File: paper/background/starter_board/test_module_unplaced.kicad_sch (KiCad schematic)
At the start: 15 parts, among them J1 Barrel_Jack_12V, M1 ERM_Motor, M2 Stepper_4wire, M3 Servo_3pin, U1 D24V22F5_Buck, U2 Pi_Pico_W, U3 DRV2605L_Breakout, U4 DRV8871_Breakout, U5 Tic_T500, U6 Waveshare_2CH_RS232

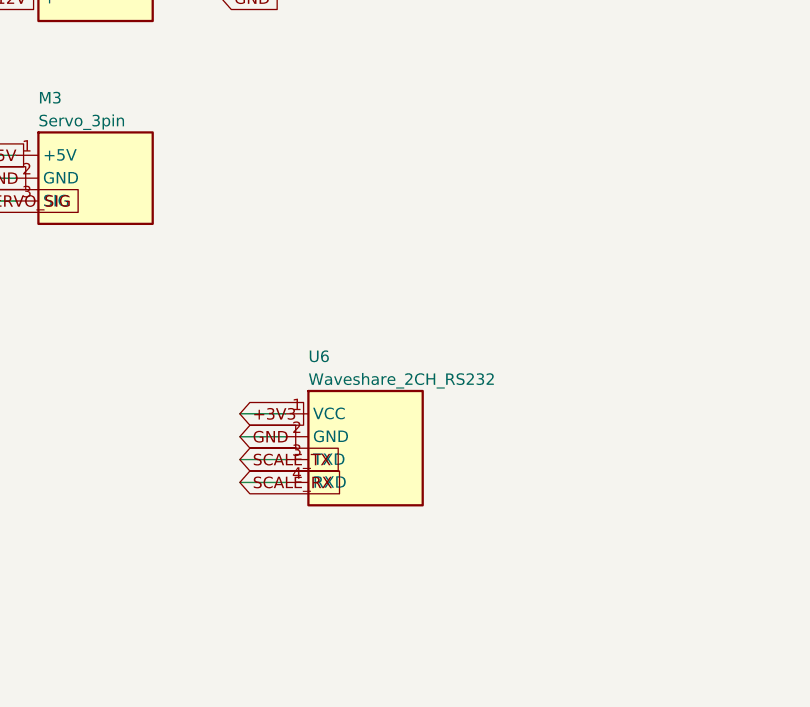
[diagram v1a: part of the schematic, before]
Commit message: Fix U6 RS-232 module footprint: restore 2x20 receptacle (mid-body 4-pin header was unpluggable)
@lbwinters caught that the generated layout placed the Waveshare
Pico-2CH-RS232 module's pin holes in the middle of its 21x52 mm body,
which would make the physical module impossible to plug in. The PR #100
alignment had adopted that PR's bench-symbol abstraction ("only its
4-pin TTL header reaches the Pico") literally, but the module's own
schematic (hardware/vendor-files/waveshare-pico-2ch-rs232) shows no
such header exists: its TTL signals live only on its 2x20
Pico-form-factor header.

U6 is again the 2x20 side receptacle the module actually plugs onto
(two real PinHeader_1x20 columns at the Pico's 17.78 mm row spacing,
as the pre-PR#100 J2 was), keeping PR #100's electrical intent:
channel 0 straight across to UART0 by board copper (GP12 -> TXD0 =
SCALE_TX, GP13 <- RXD0 = SCALE_RX), VCC (VSYS position) and the
3V3-position LED rail on +3V3, all 8 GND positions grounded,
channel 1 spare.

Board becomes 15 footprints / 137 pads / 83 net-assigned / 22 nets.
Verified: kicad-cli sch export netlist (83 pins, 22 nets, zero
unconnected, both trios), pcbnew 7.0.11 DRC (0 courtyard/clearance
errors), 15<->15 footprint<->symbol UUID bijection, byte-for-byte
reproducible, KiCad 7 20221018 format kept. Both trios + previews
regenerated; note 21, background README, and the vendor-files README
updated.

Co-authored-by: Luke Blaine Winters <288785662+lbwinters@users.noreply.github.com>
Co-Authored-By: Claude Fable 5 <noreply@anthropic.com>
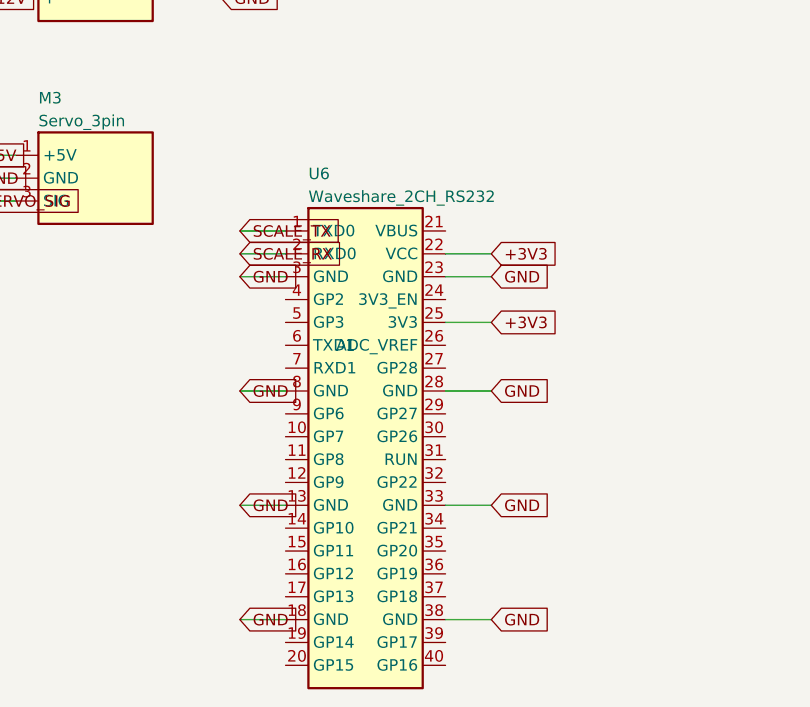
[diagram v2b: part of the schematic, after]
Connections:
- net +3V3: now also U6.22 (VCC), U6.25 (3V3); no longer U6.1 (VCC)
- net GND: now also U6.13 (GND), U6.18 (GND), U6.23 (GND), U6.28 (GND), U6.3 (GND), U6.33 (GND), U6.38 (GND), U6.8 (GND); no longer U6.2 (GND)
- net SCALE_RX: now also U6.2 (RXD0); no longer U6.4 (RXD)
- net SCALE_TX: now also U6.1 (TXD0); no longer U6.3 (TXD)
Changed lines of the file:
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@@
   (symbol (lib_id "powder_doser_parts:Waveshare_2CH_RS232") (at 240 245 0) (unit 1)
     (in_bom yes) (on_board yes) (dnp no)
-    (property "Reference" "U6" (id 0) (at 233.65 234.84 0)
+    (property "Reference" "U6" (id 0) (at 233.65 214.52 0)
       (effects (font (size 1.27 1.27)) (justify left)))
-    (property "Value" "Waveshare_2CH_RS232" (id 1) (at 233.65 237.38 0)
+    (property "Value" "Waveshare_2CH_RS232" (id 1) (at 233.65 217.06 0)
       (effects (font (size 1.27 1.27)) (justify left)))
     (property "Footprint" "powder_doser_parts:Waveshare_2CH_RS232" (id 2) (at 240 245 0)
@@
     )
   )
-  (wire (pts (xy 231.11 241.19) (xy 226.03 241.19))
+  (wire (pts (xy 231.11 220.87) (xy 226.03 220.87))
     (stroke (width 0) (type default))
   )
-  (global_label "+3V3" (shape input) (at 226.03 241.19 180) (fields_autoplaced)
+  (global_label "SCALE_TX" (shape input) (at 226.03 220.87 180) (fields_autoplaced)
     (effects (font (size 1.27 1.27)) (justify left))
   )
-  (wire (pts (xy 231.11 243.73) (xy 226.03 243.73))
+  (wire (pts (xy 231.11 223.41) (xy 226.03 223.41))
     (stroke (width 0) (type default))
   )
-  (global_label "GND" (shape input) (at 226.03 243.73 180) (fields_autoplaced)
+  (global_label "SCALE_RX" (shape input) (at 226.03 223.41 180) (fields_autoplaced)
     (effects (font (size 1.27 1.27)) (justify left))
   )
-  (wire (pts (xy 231.11 246.27) (xy 226.03 246.27))
+  (wire (pts (xy 231.11 225.95) (xy 226.03 225.95))
     (stroke (width 0) (type default))
   )
-  (global_label "SCALE_TX" (shape input) (at 226.03 246.27 180) (fields_autoplaced)
+  (global_label "GND" (shape input) (at 226.03 225.95 180) (fields_autoplaced)
     (effects (font (size 1.27 1.27)) (justify left))
   )
-  (wire (pts (xy 231.11 248.81) (xy 226.03 248.81))
+  (wire (pts (xy 231.11 238.65) (xy 226.03 238.65))
     (stroke (width 0) (type default))
   )
-  (global_label "SCALE_RX" (shape input) (at 226.03 248.81 180) (fields_autoplaced)
+  (global_label "GND" (shape input) (at 226.03 238.65 180) (fields_autoplaced)
     (effects (font (size 1.27 1.27)) (justify left))
   )
+  (wire (pts (xy 231.11 251.35) (xy 226.03 251.35))
+    (stroke (width 0) (type default))
+  )
+  (global_label "GND" (shape input) (at 226.03 251.35 180) (fields_autoplaced)
+    (effects (font (size 1.27 1.27)) (justify left))
+  )
+  (wire (pts (xy 231.11 264.05) (xy 226.03 264.05))
+    (stroke (width 0) (type default))
+  )
+  (global_label "GND" (shape input) (at 226.03 264.05 180) (fields_autoplaced)
+    (effects (font (size 1.27 1.27)) (justify left))
+  )
+  (wire (pts (xy 248.89 223.41) (xy 253.97 223.41))
+    (stroke (width 0) (type default))
+  )
+  (global_label "+3V3" (shape input) (at 253.97 223.41 0) (fields_autoplaced)
+    (effects (font (size 1.27 1.27)) (justify left))
+  )
+  (wire (pts (xy 248.89 225.95) (xy 253.97 225.95))
+    (stroke (width 0) (type default))
+  )
+  (global_label "GND" (shape input) (at 253.97 225.95 0) (fields_autoplaced)
+    (effects (font (size 1.27 1.27)) (justify left))
+  )
+  (wire (pts (xy 248.89 231.03) (xy 253.97 231.03))
+    (stroke (width 0) (type default))
+  )
+  (global_label "+3V3" (shape input) (at 253.97 231.03 0) (fields_autoplaced)
+    (effects (font (size 1.27 1.27)) (justify left))
+  )
+  (wire (pts (xy 248.89 238.65) (xy 253.97 238.65))
+    (stroke (width 0) (type default))
+  )
+  (global_label "GND" (shape input) (at 253.97 238.65 0) (fields_autoplaced)
+    (effects (font (size 1.27 1.27)) (justify left))
+  )
+  (wire (pts (xy 248.89 251.35) (xy 253.97 251.35))
+    (stroke (width 0) (type default))
+  )
+  (global_label "GND" (shape input) (at 253.97 251.35 0) (fields_autoplaced)
+    (effects (font (size 1.27 1.27)) (justify left))
+  )
+  (wire (pts (xy 248.89 264.05) (xy 253.97 264.05))
+    (stroke (width 0) (type default))
+  )
+  (global_label "GND" (shape input) (at 253.97 264.05 0) (fields_autoplaced)
+    (effects (font (size 1.27 1.27)) (justify left))
+  )

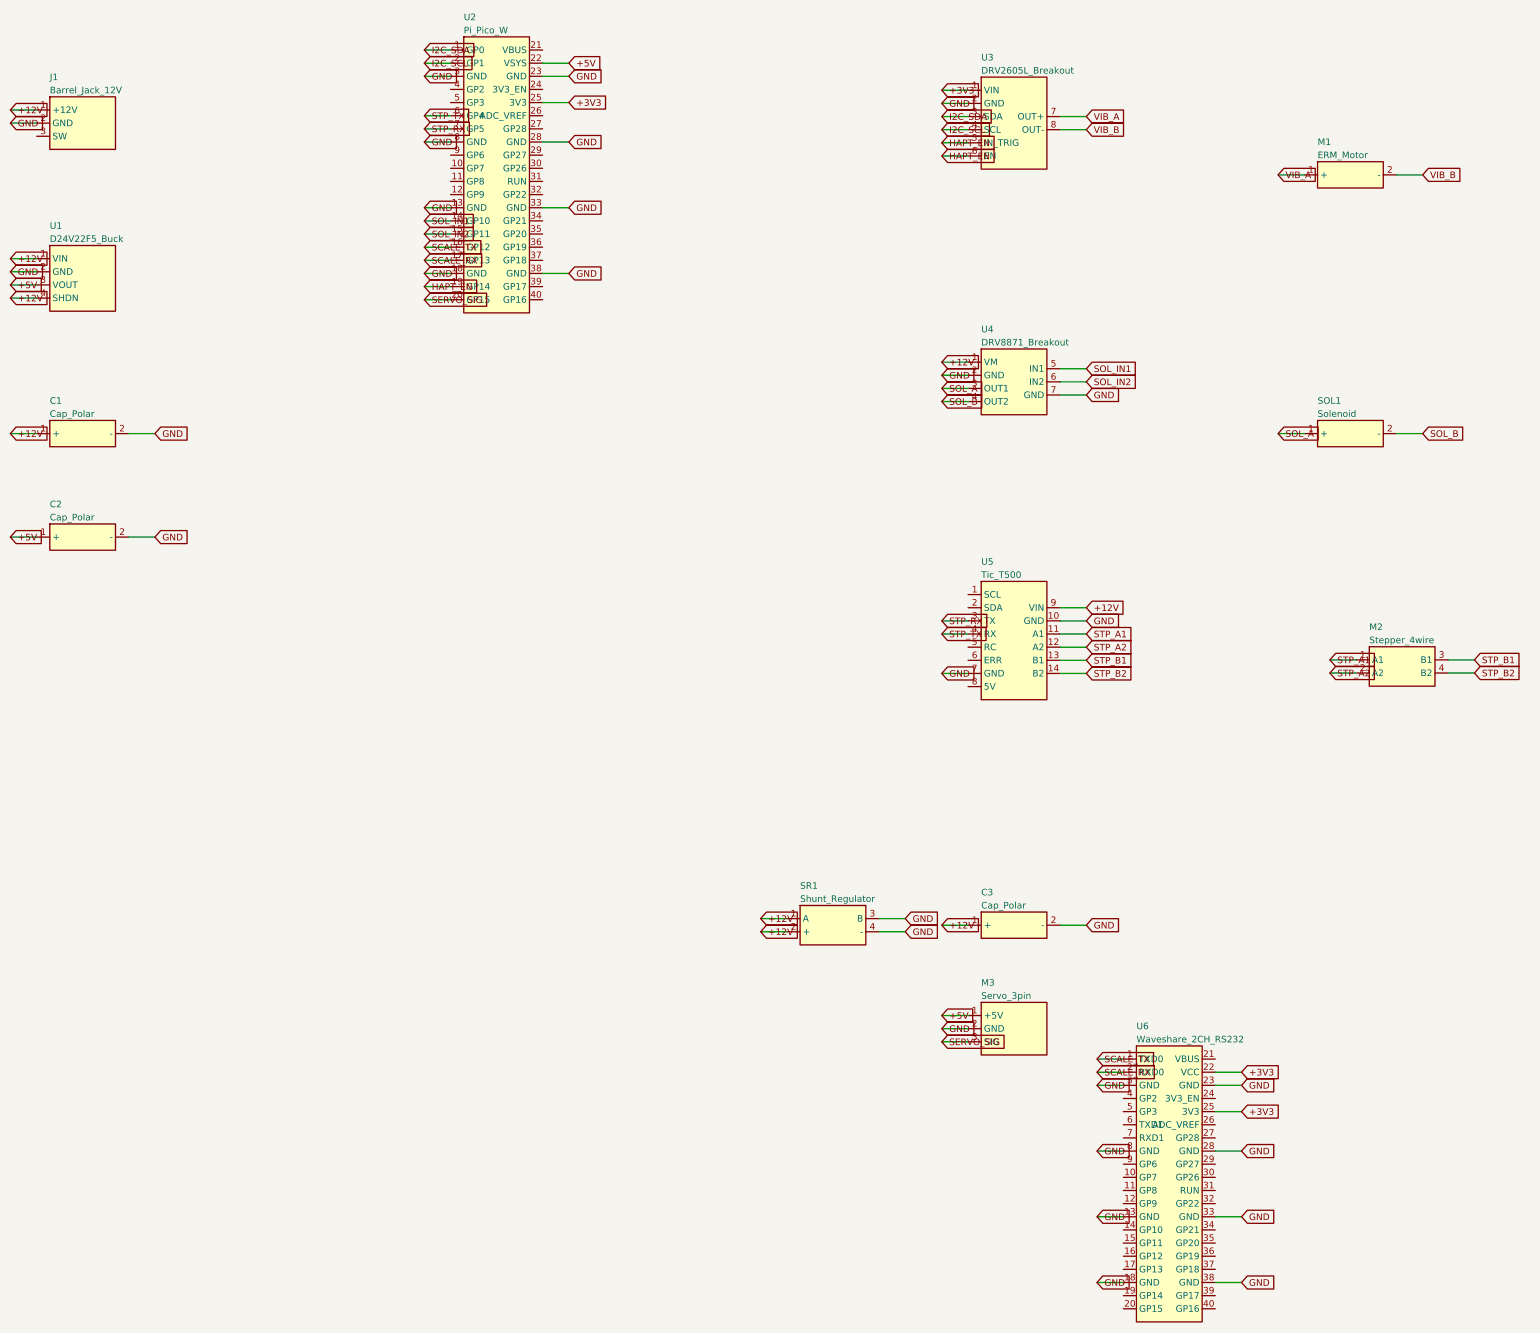
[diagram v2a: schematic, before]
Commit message: Full physical-footprint audit: vendor-exact hole maps for all 5 carriers + barrel-jack GND fix
Re-verified every component against primary vendor geometry (PR #25 Eagle
.brd files, Pololu reg19a/tvs01a/tic03b dimension diagrams + official
tic03b drill-guide DXF, CUI PJ-102AH datasheet, Waveshare module schematic,
Pico mechanical drawing) per PR #76 review request. Fixes five unpluggable
land patterns (Tic T500 38.1x26.7 mm with all 29 real holes and correct
A2/A1 order; D24V22F5 17.8x17.8 mm PG/EN/VIN/GND/VOUT row + offset GND;
shunt regulator 28.6x20.3 mm wire terminals; DRV8871 3.5 mm terminal
blocks + 1x4 logic header; DRV2605L STEMMA QT 1x5 row with real SCL/SDA
order, EN pin dropped as nonexistent) and one wiring fault (barrel-jack
GND was on the switch lug, which floats when a plug is inserted; now on
the sleeve). Boards grow to 172 pads / 95 net-assigned / 22 nets; the
unplaced auto-place outline is re-sized 100x100 -> 110x110 mm to stay in
the 35-55% utilisation band with the real bodies. kicad-cli netlist
(95 pins, zero unconnected), pcbnew DRC (no courtyard/clearance/short
errors), 15<->15 footprint<->symbol UUID bijection, and byte-for-byte
reproducibility all re-verified on both trios.

Co-authored-by: Luke Blaine Winters <288785662+lbwinters@users.noreply.github.com>
Co-Authored-By: Claude Fable 5 <noreply@anthropic.com>
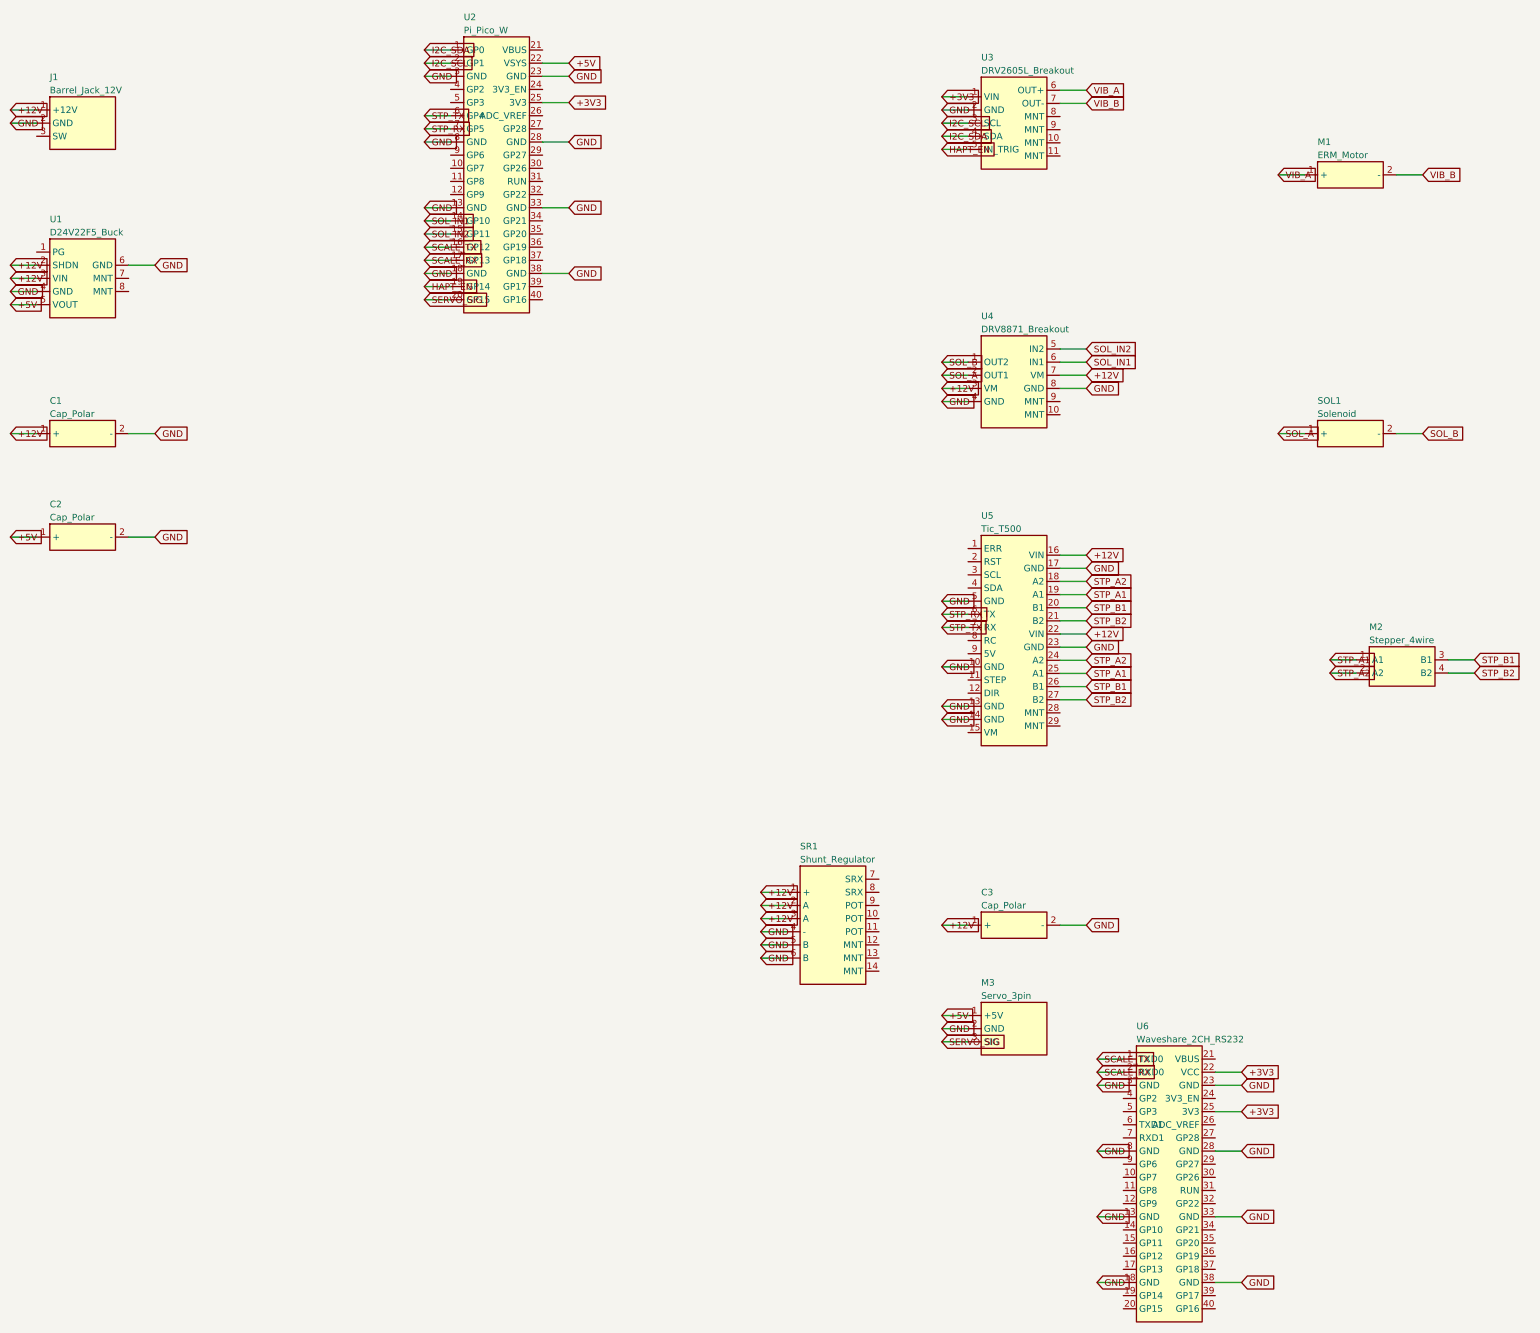
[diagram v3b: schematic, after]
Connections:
- net +12V: now also SR1.3 (A), U1.2 (SHDN), U1.3 (VIN), U4.3 (VM), U4.7 (VM), U5.16 (VIN), U5.22 (VIN); no longer U1.1 (VIN), U1.4 (SHDN), U4.1 (VM), U5.9 (VIN)
- net +5V: now also U1.5 (VOUT); no longer U1.3 (VOUT)
- net GND: now also SR1.5 (B), SR1.6 (B), U1.4 (GND), U1.6 (GND), U4.4 (GND), U4.8 (GND), U5.13 (GND), U5.14 (GND), U5.17 (GND), U5.23 (GND), U5.5 (GND); no longer SR1.3 (B), U1.2 (GND), U4.2 (GND), U4.7 (GND), U5.7 (GND)
- net HAPT_EN: no longer U3.6 (EN)
- net I2C_SCL: now also U3.3 (SCL); no longer U3.4 (SCL)
- net I2C_SDA: now also U3.4 (SDA); no longer U3.3 (SDA)
- net SOL_A: now also U4.2 (OUT1); no longer U4.3 (OUT1)
- net SOL_B: now also U4.1 (OUT2); no longer U4.4 (OUT2)
- net SOL_IN1: now also U4.6 (IN1); no longer U4.5 (IN1)
- net SOL_IN2: now also U4.5 (IN2); no longer U4.6 (IN2)
- net STP_A1: now also U5.19 (A1), U5.25 (A1); no longer U5.11 (A1)
- net STP_A2: now also U5.18 (A2), U5.24 (A2); no longer U5.12 (A2)
- net STP_B1: now also U5.20 (B1), U5.26 (B1); no longer U5.13 (B1)
- net STP_B2: now also U5.21 (B2), U5.27 (B2); no longer U5.14 (B2)
- net STP_RX: now also U5.6 (TX); no longer U5.3 (TX)
- net STP_TX: now also U5.7 (RX); no longer U5.4 (RX)
- net VIB_A: now also U3.6 (OUT+); no longer U3.7 (OUT+)
- net VIB_B: now also U3.7 (OUT-); no longer U3.8 (OUT-)
